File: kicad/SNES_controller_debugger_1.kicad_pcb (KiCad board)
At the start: 2 copper layers, 100 x 74 mm, 32 parts, among them J1 ICSP, J2 CONTROLLER OUT, J3 MICRO_USB, Q1 DMG2302UK-7, Q2 DMP2215L-7, SW1 Reset, U1 ATmega32U4, Y1 16MHz

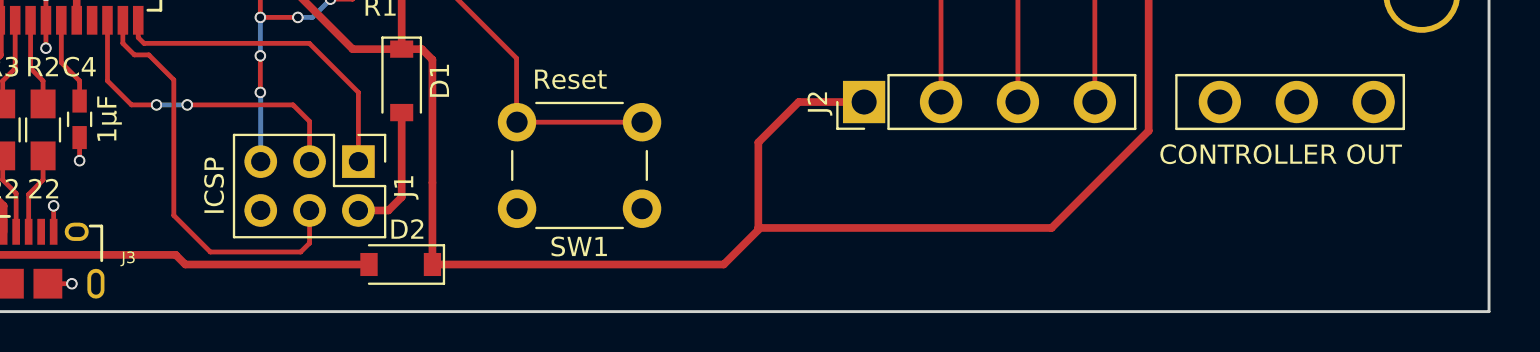
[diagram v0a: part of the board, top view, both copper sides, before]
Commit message: pcb: Fix/add some footprints
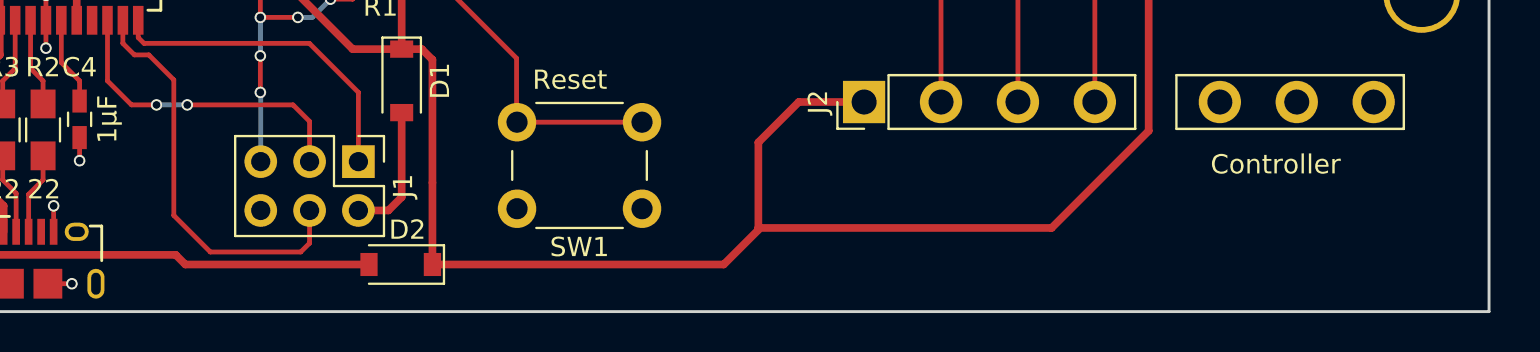
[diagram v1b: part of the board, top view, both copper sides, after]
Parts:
- H1, H2, H3, H4: value MountingHole_3.4mm -> (none)
- J2: value CONTROLLER OUT -> Controller
